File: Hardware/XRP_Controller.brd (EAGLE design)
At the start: 63.5 x 54 mm, 222 parts, among them J1 POWER_JACKPOWER_JACK_SLOT, J12 Vertical Qwiic Connector, J13 Vertical Qwiic Connector, J14 Vertical Qwiic Connector, J3 JST_6_PIN_VERTICAL, J4 JST_6_PIN_VERTICAL, J5 JST_6_PIN_VERTICAL, J6 JST_6_PIN_VERTICAL, J9 Vertical Qwiic Connector, Q3 20V/4.2A/52mΩ/1.4W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

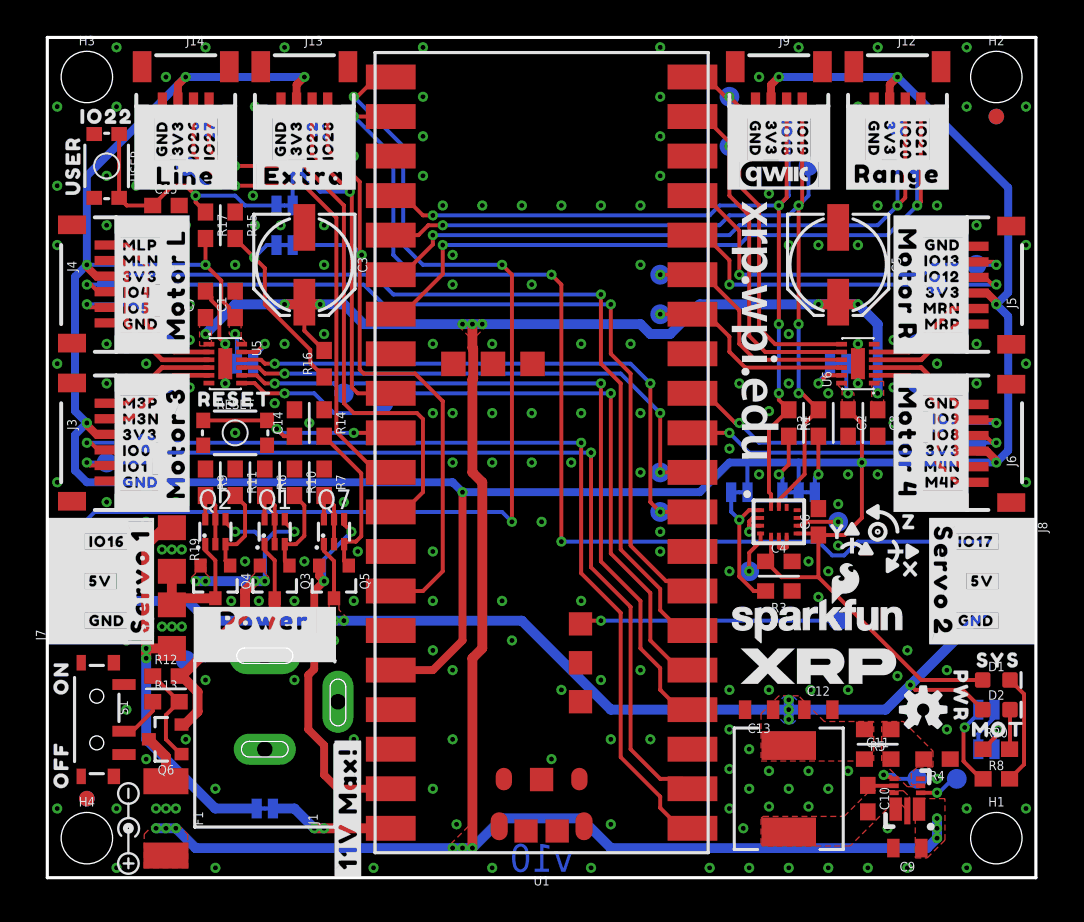
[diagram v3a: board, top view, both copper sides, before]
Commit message: Minor tweaks
Update buck footprint to link to SFE Eagle library
Change motor nets and silk labels to use +/- instead of P/N
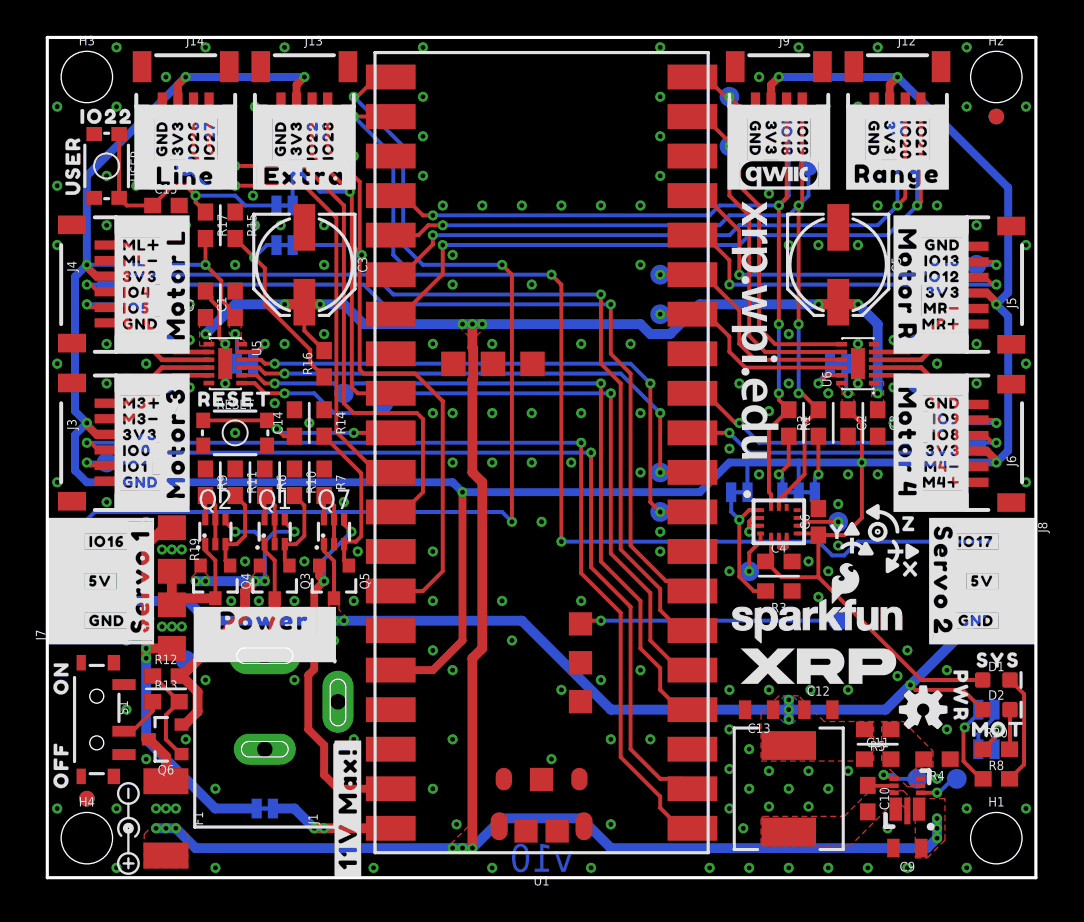
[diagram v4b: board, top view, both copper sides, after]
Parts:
- removed U$36: (no value), output:#M4P#0
- removed U$37: (no value), output:#M4N#0
- added U$94: (no value), output:#M3##0
- added U$99: (no value), output:#M3##4
- U$14: device output:#MLN#0 -> output:#MR##1
- U$16: device output:#M3N#0 -> output:#ML##0
- U$18: device output:#MRN#0 -> output:#M4##0
- U$19: device output:#MRP#0 -> output:#M4##5
- U$32: device output:#M3P#0 -> output:#ML##1
- U$9: device output:#MLP#0 -> output:#MR##0
- U2: device Buck5V:V-DFN3020-13 -> SparkFun-IC-Power:V-DFN3020-13
- moved U$9 55.1 mm to (59.2, 35.6)
- moved U$14 54.9 mm to (59.2, 36.6)
- moved U$16 11.2 mm to (4.32, 40.6)
- moved U$18 11.2 mm to (59.2, 25.4)
- moved U$19 9.14 mm to (59.2, 26.4)
- moved U$32 9.14 mm to (4.32, 39.6)
- moved U$90 0.13 mm to (55.4, 22.7)
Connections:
- net MOT_3_N renamed MOT_3-
- net MOT_3_P renamed MOT_3+
- net MOT_4_N renamed MOT_4-
- net MOT_4_P renamed MOT_4+
- net MOT_L_N renamed MOT_L-
- net MOT_L_P renamed MOT_L+
- net MOT_R_N renamed MOT_R-
- net MOT_R_P renamed MOT_R+
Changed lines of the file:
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@@
 <rectangle x1="4.318" y1="23.495" x2="7.62" y2="24.892" layer="21"/>
 <rectangle x1="4.318" y1="24.892" x2="4.699" y2="30.988" layer="21"/>
-<rectangle x1="7.112" y1="24.892" x2="7.62" y2="30.988" layer="21"/>
-<rectangle x1="6.731" y1="25.908" x2="7.112" y2="27.94" layer="21"/>
+<rectangle x1="7.239" y1="24.892" x2="7.62" y2="30.988" layer="21"/>
+<rectangle x1="6.731" y1="25.908" x2="7.239" y2="27.94" layer="21"/>
 <rectangle x1="6.731" y1="36.068" x2="7.239" y2="38.1" layer="21"/>
-<rectangle x1="56.261" y1="27.94" x2="56.642" y2="29.972" layer="21"/>
+<rectangle x1="56.2356" y1="27.94" x2="56.642" y2="29.972" layer="21"/>
 <rectangle x1="56.642" y1="45.847" x2="57.912" y2="49.657" layer="21"/>
 <rectangle x1="51.308" y1="45.847" x2="52.578" y2="49.657" layer="21"/>
@@
 <rectangle x1="55.88" y1="41.148" x2="59.182" y2="42.545" layer="21" rot="R180"/>
 <rectangle x1="58.801" y1="35.052" x2="59.182" y2="41.148" layer="21" rot="R180"/>
-<rectangle x1="55.88" y1="35.052" x2="56.261" y2="41.148" layer="21" rot="R180"/>
+<rectangle x1="55.88" y1="35.052" x2="56.134" y2="41.148" layer="21"/>
 <rectangle x1="54.356" y1="42.037" x2="55.88" y2="42.545" layer="21" rot="R180"/>
 <rectangle x1="54.356" y1="33.655" x2="55.88" y2="34.163" layer="21" rot="R180"/>
@@
 <rectangle x1="55.88" y1="30.988" x2="59.182" y2="32.385" layer="21" rot="R180"/>
 <rectangle x1="58.801" y1="24.892" x2="59.182" y2="30.988" layer="21" rot="R180"/>
-<rectangle x1="55.88" y1="24.892" x2="56.261" y2="30.988" layer="21" rot="R180"/>
+<rectangle x1="55.88" y1="24.892" x2="56.2356" y2="30.988" layer="21"/>
 <rectangle x1="54.356" y1="31.877" x2="55.88" y2="32.385" layer="21" rot="R180"/>
 <rectangle x1="54.356" y1="23.495" x2="55.88" y2="24.003" layer="21" rot="R180"/>
@@
 <rectangle x1="14.478" y1="48.768" x2="18.542" y2="49.657" layer="21"/>
 <rectangle x1="14.478" y1="45.847" x2="18.542" y2="46.101" layer="21"/>
-<rectangle x1="51.308" y1="44.323" x2="51.435" y2="45.847" layer="21"/>
-<rectangle x1="57.785" y1="44.323" x2="57.912" y2="45.847" layer="21"/>
-<rectangle x1="51.308" y1="44.196" x2="55.372" y2="44.323" layer="21"/>
+<rectangle x1="51.308" y1="44.2468" x2="51.435" y2="45.847" layer="21"/>
+<rectangle x1="57.785" y1="44.2468" x2="57.912" y2="45.847" layer="21"/>
+<rectangle x1="51.308" y1="44.196" x2="57.912" y2="44.2468" layer="21"/>
 <rectangle x1="10.922" y1="45.847" x2="12.192" y2="49.657" layer="21"/>
 <rectangle x1="5.588" y1="45.847" x2="6.858" y2="49.657" layer="21"/>
@@
 <rectangle x1="39.243" y1="31.623" x2="39.624" y2="31.877" layer="41"/>
 <rectangle x1="17.653" y1="16.129" x2="17.907" y2="16.256" layer="41"/>
-<rectangle x1="56.007" y1="44.196" x2="57.912" y2="44.323" layer="21"/>
-<rectangle x1="55.372" y1="44.196" x2="56.007" y2="44.2468" layer="21"/>
 <rectangle x1="52.197" y1="6.604" x2="52.324" y2="6.858" layer="41"/>
 <text x="31.75" y="1.27" size="1.778" layer="22" font="vector" ratio="15" rot="MR0" align="center">v10</text>
@@
 <attribute name="VALUE" x="52.578" y="29.21" size="0.6096" layer="27" font="vector" ratio="20" rot="R270" align="top-center"/>
 </element>
-<element name="U2" library="Buck5V" package="V-DFN3020-13" value="AP63357" x="55.245" y="5.08" smashed="yes" rot="R90">
+<element name="U2" library="SparkFun-IC-Power" package="V-DFN3020-13" value="AP63357" x="55.245" y="5.08" smashed="yes" rot="R90">
 <attribute name="PN" value="AP63357DV-7" x="55.245" y="5.08" size="1.778" layer="27" font="vector" ratio="15" rot="R90" display="off"/>
 <attribute name="PROD_ID" value="VREG-17224" x="55.245" y="5.08" size="1.778" layer="27" font="vector" ratio="15" rot="R90" display="off"/>
@@
 <element name="U$34" library="output" package="#IO12#0" value="" x="59.182" y="38.608" smashed="yes"/>
 <element name="U$35" library="output" package="#IO13#0" value="" x="59.182" y="39.624" smashed="yes"/>
-<element name="U$36" library="output" package="#M4P#0" value="" x="59.182" y="25.4" smashed="yes"/>
-<element name="U$37" library="output" package="#M4N#0" value="" x="59.182" y="26.416" smashed="yes"/>
 <element name="U$38" library="output" package="#IO27#0" value="" x="10.414" y="49.149" smashed="yes" rot="R90"/>
 <element name="U$39" library="output" package="#IO28#0" value="" x="18.034" y="49.149" smashed="yes" rot="R90"/>
@@
 <element name="U$88" library="output" package="X0" value="" x="55.499" y="19.812" smashed="yes"/>
 <element name="U$89" library="output" package="Y0" value="" x="50.8" y="22.225" smashed="yes"/>
-<element name="U$90" library="output" package="Z0" value="" x="55.372" y="22.86" smashed="yes"/>
+<element name="U$90" library="output" package="Z0" value="" x="55.372" y="22.733" smashed="yes"/>
 <element name="U$64" library="output" package="#IMU_ADR#0" value="" x="43.561" y="24.765" smashed="yes" rot="MR0"/>
 <element name="LOGO4" library="SparkFun-Aesthetics" package="SFE_LOGO_NAME_FLAME_.1" value="SFE_LOGO_NAME_FLAME.1_INCH" x="49.53" y="16.51" smashed="yes"/>
@@
 </element>
 <element name="TP2" library="SparkFun-Connectors" package="PAD.03X.05" value="TEST-POINT3X5" x="3.81" y="26.67" smashed="yes" rot="MR0"/>
-<element name="U$9" library="output" package="#MLP#0" value="" x="4.318" y="40.64" smashed="yes"/>
-<element name="U$14" library="output" package="#MLN#0" value="" x="4.318" y="39.624" smashed="yes"/>
-<element name="U$16" library="output" package="#M3N#0" value="" x="4.318" y="29.464" smashed="yes"/>
-<element name="U$32" library="output" package="#M3P#0" value="" x="4.318" y="30.48" smashed="yes"/>
-<element name="U$18" library="output" package="#MRN#0" value="" x="59.182" y="36.576" smashed="yes"/>
-<element name="U$19" library="output" package="#MRP#0" value="" x="59.182" y="35.56" smashed="yes"/>
 <element name="TP3" library="SparkFun-Connectors" package="PAD.03X.05" value="TEST-POINT3X5" x="19.05" y="31.115" smashed="yes" rot="MR0"/>
 <element name="TP4" library="SparkFun-Connectors" package="PAD.03X.05" value="TEST-POINT3X5" x="21.59" y="30.48" smashed="yes" rot="MR0"/>
@@
 <element name="U$72" library="XRP_COMPONENTS" package="XRP_URL_3MM" value="" x="45.466" y="35.179" smashed="yes" rot="R270"/>
 <element name="U$97" library="XRP_COMPONENTS" package="XRP_URL_5MM" value="" x="20.574" y="22.733" smashed="yes" rot="MR0"/>
+<element name="U$94" library="output" package="#M3##0" value="" x="4.318" y="30.48" smashed="yes"/>
+<element name="U$99" library="output" package="#M3##4" value="" x="4.318" y="29.464" smashed="yes"/>
+<element name="U$16" library="output" package="#ML##0" value="" x="4.318" y="40.64" smashed="yes"/>
+<element name="U$32" library="output" package="#ML##1" value="" x="4.318" y="39.624" smashed="yes"/>
+<element name="U$9" library="output" package="#MR##0" value="" x="59.182" y="35.56" smashed="yes"/>
+<element name="U$14" library="output" package="#MR##1" value="" x="59.182" y="36.576" smashed="yes"/>
+<element name="U$18" library="output" package="#M4##0" value="" x="59.182" y="25.4" smashed="yes"/>
+<element name="U$19" library="output" package="#M4##5" value="" x="59.182" y="26.416" smashed="yes"/>
 </elements>
 <signals>
@@
 <contactref element="U1" pad="15"/>
 </signal>
-<signal name="MOT_3_P">
+<signal name="MOT_3+">
 <contactref element="J3" pad="1"/>
 <contactref element="U5" pad="4"/>
@@
 <wire x1="5.08" y1="31.75" x2="5.715" y2="31.115" width="0.254" layer="1"/>
 </signal>
-<signal name="MOT_3_N">
+<signal name="MOT_3-">
 <contactref element="J3" pad="2"/>
 <contactref element="U5" pad="5"/>
@@
 <via x="7.62" y="31.75" extent="1-16" drill="0.3048"/>
 </signal>
-<signal name="MOT_L_P">
+<signal name="MOT_L+">
 <contactref element="J4" pad="1"/>
 <contactref element="U5" pad="2"/>
@@
 <via x="7.62" y="34.29" extent="1-16" drill="0.3048"/>
 </signal>
-<signal name="MOT_L_N">
+<signal name="MOT_L-">
 <contactref element="J4" pad="2"/>
 <contactref element="U5" pad="3"/>
@@
 <wire x1="5.08" y1="34.29" x2="5.715" y2="34.925" width="0.254" layer="1"/>
 </signal>
-<signal name="MOT_R_P">
+<signal name="MOT_R+">
 <contactref element="J5" pad="1"/>
 <contactref element="U6" pad="4"/>
@@
 <wire x1="58.42" y1="34.29" x2="57.785" y2="34.925" width="0.254" layer="1"/>
 </signal>
-<signal name="MOT_R_N">
+<signal name="MOT_R-">
 <contactref element="J5" pad="2"/>
 <contactref element="U6" pad="5"/>
@@
 <via x="55.88" y="34.29" extent="1-16" drill="0.3048"/>
 </signal>
-<signal name="MOT_4_P">
+<signal name="MOT_4+">
 <contactref element="J6" pad="1"/>
 <contactref element="U6" pad="2"/>
@@
 <via x="55.88" y="31.75" extent="1-16" drill="0.3048"/>
 </signal>
-<signal name="MOT_4_N">
+<signal name="MOT_4-">
 <contactref element="J6" pad="2"/>
 <contactref element="U6" pad="3"/>

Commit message: Add ordering instructions
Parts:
- added U$36: (no value), SparkFun-Aesthetics:ORDERING_INSTRUCTIONS
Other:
- board text added: "Solder Mask: Red Thickness: 1.6mm Two layer design Finish: Lead Free HASL"
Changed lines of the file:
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@@
 <rectangle x1="52.197" y1="6.604" x2="52.324" y2="6.858" layer="41"/>
 <text x="31.75" y="1.27" size="1.778" layer="22" font="vector" ratio="15" rot="MR0" align="center">v10</text>
+<text x="73.66" y="39.37" size="1.778" layer="51" font="vector" ratio="15" align="top-left">Solder Mask: Red
+Thickness: 1.6mm
+Two layer design
+Finish: Lead Free HASL</text>
 </plain>
 <attributes>
@@
 <element name="U$18" library="output" package="#M4##0" value="" x="59.182" y="25.4" smashed="yes"/>
 <element name="U$19" library="output" package="#M4##5" value="" x="59.182" y="26.416" smashed="yes"/>
+<element name="U$36" library="SparkFun-Aesthetics" package="ORDERING_INSTRUCTIONS" value="" x="71.12" y="50.8" smashed="yes"/>
 </elements>
 <signals>
@@
 </drawing>
 <compatibility>
+<note version="6.3" minversion="6.2.2" severity="warning">
+Since Version 6.2.2 text objects can contain more than one line,
+which will not be processed correctly with this version.
+</note>
 <note version="8.3" severity="warning">
 Since Version 8.3, EAGLE supports URNs for individual library

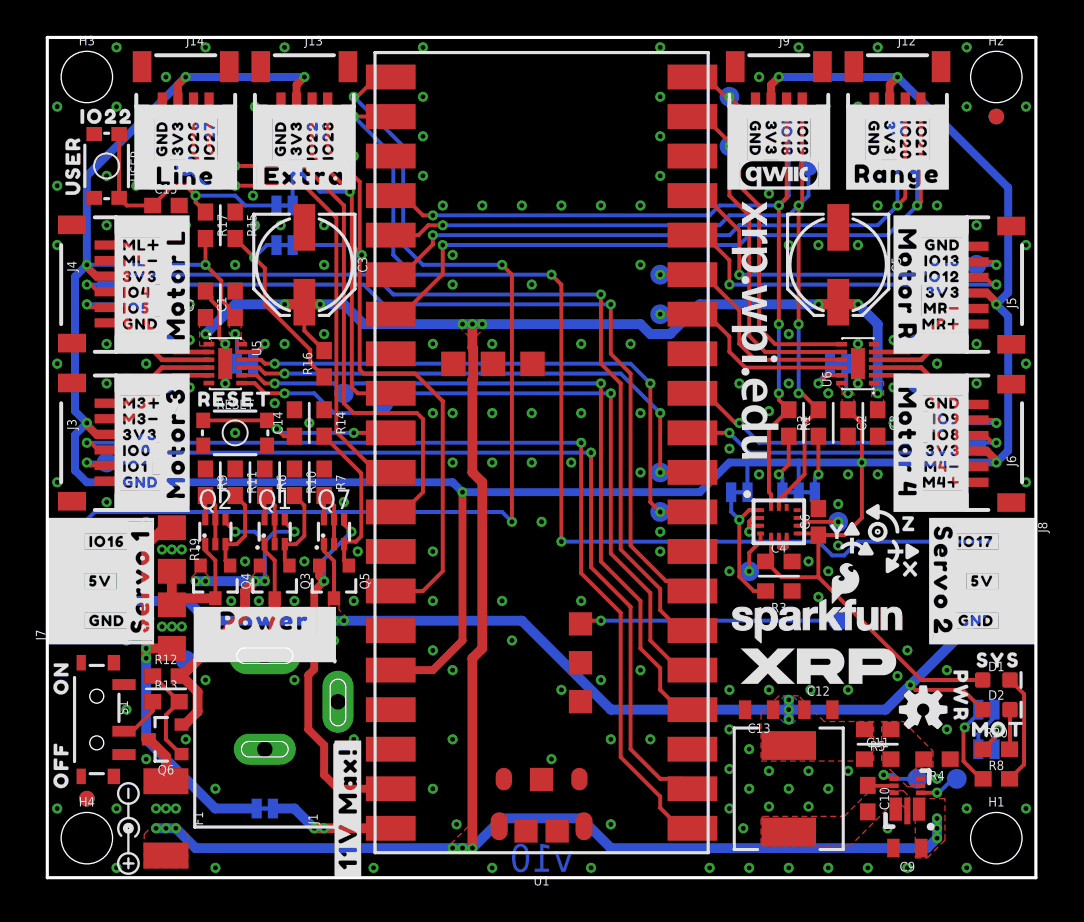
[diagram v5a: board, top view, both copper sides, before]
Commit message: Move user button
Corner was not accessible enough in chassis. User button now takes the location of the XRP logo just under the SparkFun logo
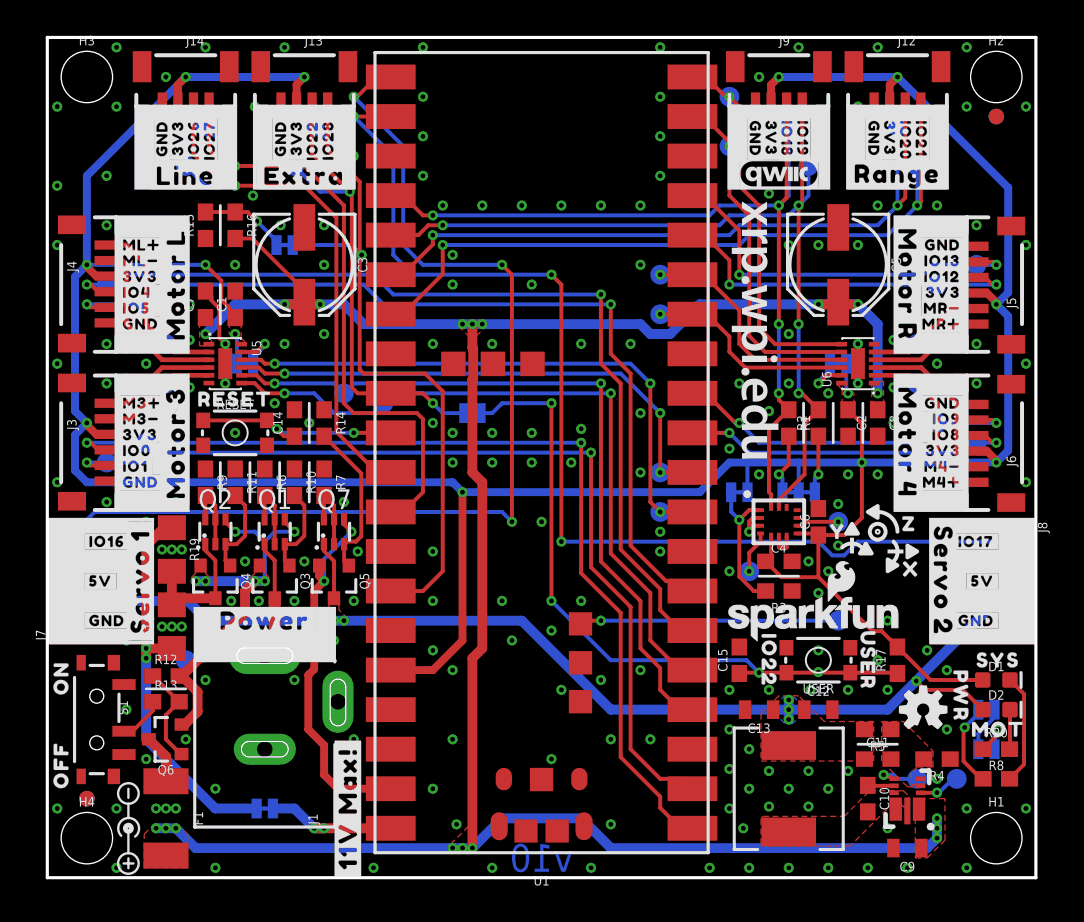
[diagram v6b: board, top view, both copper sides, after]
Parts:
- removed U$65: (no value), XRP_LOGOS:XRP_LOGO
- moved U$83 60.1 mm to (52.7, 14.0), turned to 270 degrees
- moved USER 55.7 mm to (49.5, 14.0), turned to 180 degrees
- moved U$68 55.0 mm to (46.4, 14.0), turned to 270 degrees
- moved R17 52.5 mm to (54.6, 14.0), turned to 90 degrees
- moved C15 47.0 mm to (44.5, 14.0), turned to 90 degrees
- moved U$84 19.2 mm to (28.2, 29.8)
- moved USER_BTN 18.0 mm to (27.3, 29.8), turned to 0 degrees
- moved R16 10.6 mm to (12.1, 41.9), turned to 270 degrees
- moved R15 1.90 mm to (10.2, 41.9), turned to 90 degrees
- moved LOGO4 0.28 mm to (49.3, 16.6)
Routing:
- net N$17: track 16.8 -> 43.0 mm, vias 1 -> 4
- net N$12: track 13.0 -> 5.59 mm
- net VIN: track 147.2 -> 150.2 mm
- net RP_IO22/USER_BTN: track 28.7 -> 31.4 mm, vias 1 -> 2
- net 3.3V: track 217.4 -> 215.8 mm
- net GND: vias 204 -> 206
